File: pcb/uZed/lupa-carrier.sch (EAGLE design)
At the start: 94 parts, among them J5 HDMI-TYPE-A-RECEPTICALFCI1002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, J6 HDMI-TYPE-A-RECEPTICALFCI1002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, K1 694108105102

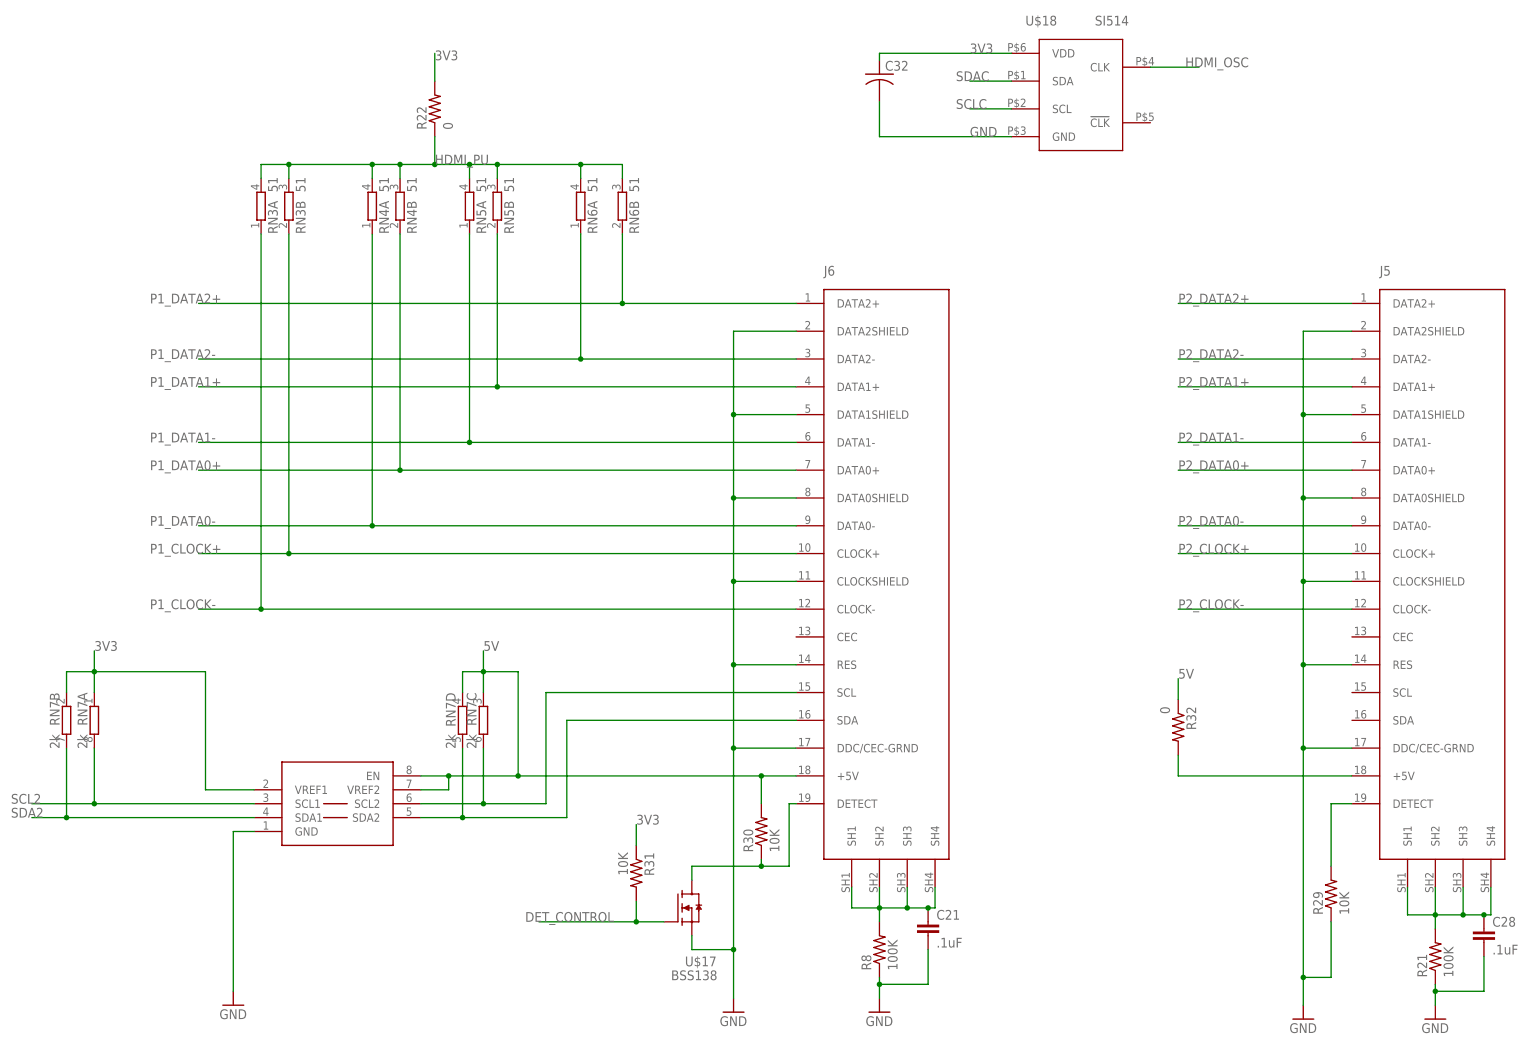
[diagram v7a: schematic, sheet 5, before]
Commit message: routing completed. needs double check before ordering from fab
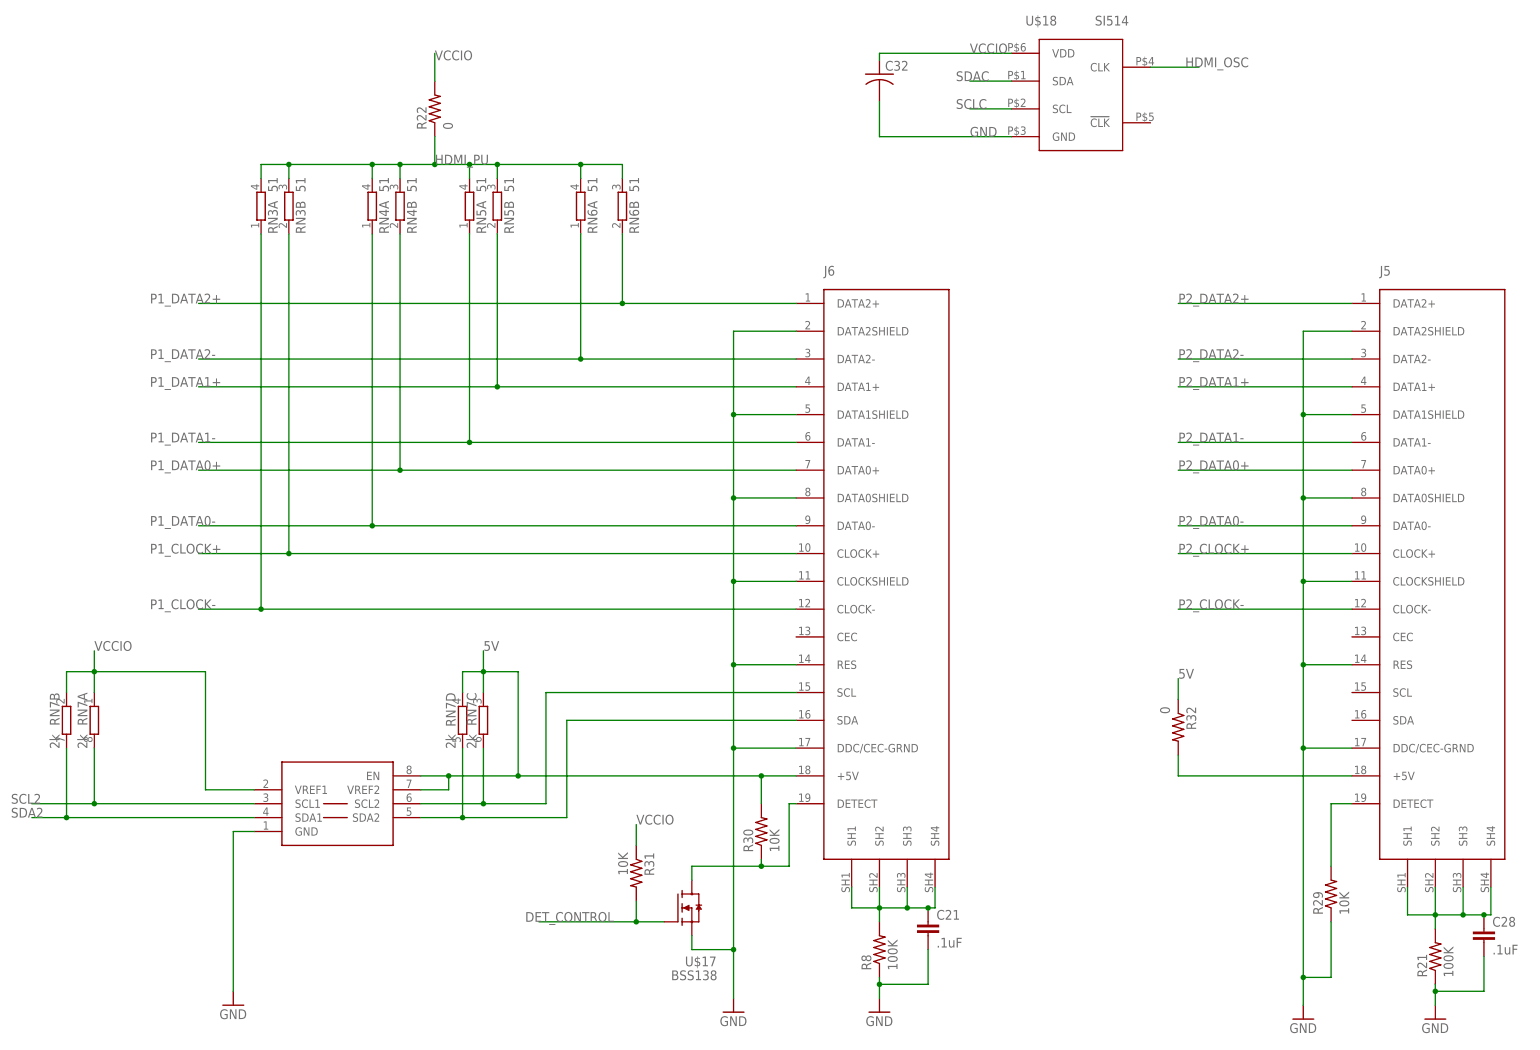
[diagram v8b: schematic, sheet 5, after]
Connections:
- removed net 3V3: C32.1, PCA9306.VREF1, R22.2, R31.1, RN7A.1, RN7B.1, U$18.VDD
- net SCLC: now also JX1.P$19
- net SDAC: now also JX1.P$17
- net VCCIO: now also C32.1, PCA9306.VREF1, R22.2, R31.1, RN7A.1, RN7B.1, U$18.VDD
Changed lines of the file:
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@@
+</segment>
+</net>
+<net name="SDAC" class="0">
+<segment>
+<pinref part="JX1" gate="G$1" pin="P$17"/>
+<wire x1="170.18" y1="129.54" x2="187.96" y2="129.54" width="0.1524" layer="91"/>
+<label x="187.96" y="129.54" size="1.778" layer="95"/>
+</segment>
+</net>
+<net name="SCLC" class="0">
+<segment>
+<pinref part="JX1" gate="G$1" pin="P$19"/>
+<wire x1="170.18" y1="127" x2="187.96" y2="127" width="0.1524" layer="91"/>
+<label x="187.96" y="127" size="1.778" layer="95"/>
 </segment>
 </net>
@@
 </segment>
 </net>
-<net name="3V3" class="0">
-<segment>
-<pinref part="R22" gate="G$1" pin="2"/>
-<wire x1="82.55" y1="185.42" x2="82.55" y2="190.5" width="0.1524" layer="91"/>
-<label x="82.55" y="189.23" size="1.778" layer="95"/>
-</segment>
-<segment>
-<pinref part="PCA9306" gate="G$1" pin="VREF1"/>
-<wire x1="49.53" y1="55.88" x2="40.64" y2="55.88" width="0.1524" layer="91"/>
-<wire x1="15.24" y1="73.66" x2="15.24" y2="77.47" width="0.1524" layer="91"/>
-<wire x1="15.24" y1="77.47" x2="20.32" y2="77.47" width="0.1524" layer="91"/>
-<wire x1="20.32" y1="77.47" x2="20.32" y2="73.66" width="0.1524" layer="91"/>
-<wire x1="20.32" y1="77.47" x2="40.64" y2="77.47" width="0.1524" layer="91"/>
-<wire x1="40.64" y1="77.47" x2="40.64" y2="55.88" width="0.1524" layer="91"/>
-<pinref part="RN7" gate="B" pin="1"/>
-<pinref part="RN7" gate="A" pin="1"/>
-<junction x="20.32" y="77.47"/>
-<wire x1="20.32" y1="77.47" x2="20.32" y2="81.28" width="0.1524" layer="91"/>
-<label x="20.32" y="81.28" size="1.778" layer="95"/>
-</segment>
-<segment>
-<pinref part="R31" gate="G$1" pin="1"/>
-<wire x1="119.38" y1="45.72" x2="119.38" y2="49.53" width="0.1524" layer="91"/>
-<label x="119.38" y="49.53" size="1.778" layer="95"/>
-</segment>
-<segment>
-<pinref part="U$18" gate="G$1" pin="VDD"/>
-<label x="180.34" y="190.5" size="1.778" layer="95"/>
-<wire x1="187.96" y1="190.5" x2="163.83" y2="190.5" width="0.1524" layer="91"/>
-<pinref part="C32" gate="G$1" pin="1"/>
-<wire x1="163.83" y1="190.5" x2="163.83" y2="189.23" width="0.1524" layer="91"/>
-</segment>
-</net>
 <net name="N$17" class="0">
 <segment>
@@
 </segment>
 </net>
+<net name="VCCIO" class="0">
+<segment>
+<pinref part="U$18" gate="G$1" pin="VDD"/>
+<label x="180.34" y="190.5" size="1.778" layer="95"/>
+<wire x1="187.96" y1="190.5" x2="163.83" y2="190.5" width="0.1524" layer="91"/>
+<pinref part="C32" gate="G$1" pin="1"/>
+<wire x1="163.83" y1="190.5" x2="163.83" y2="189.23" width="0.1524" layer="91"/>
+</segment>
+<segment>
+<pinref part="PCA9306" gate="G$1" pin="VREF1"/>
+<wire x1="49.53" y1="55.88" x2="40.64" y2="55.88" width="0.1524" layer="91"/>
+<wire x1="15.24" y1="73.66" x2="15.24" y2="77.47" width="0.1524" layer="91"/>
+<wire x1="15.24" y1="77.47" x2="20.32" y2="77.47" width="0.1524" layer="91"/>
+<wire x1="20.32" y1="77.47" x2="20.32" y2="73.66" width="0.1524" layer="91"/>
+<wire x1="20.32" y1="77.47" x2="40.64" y2="77.47" width="0.1524" layer="91"/>
+<wire x1="40.64" y1="77.47" x2="40.64" y2="55.88" width="0.1524" layer="91"/>
+<pinref part="RN7" gate="B" pin="1"/>
+<pinref part="RN7" gate="A" pin="1"/>
+<junction x="20.32" y="77.47"/>
+<wire x1="20.32" y1="77.47" x2="20.32" y2="81.28" width="0.1524" layer="91"/>
+<label x="20.32" y="81.28" size="1.778" layer="95"/>
+</segment>
+<segment>
+<pinref part="R31" gate="G$1" pin="1"/>
+<wire x1="119.38" y1="45.72" x2="119.38" y2="49.53" width="0.1524" layer="91"/>
+<label x="119.38" y="49.53" size="1.778" layer="95"/>
+</segment>
+<segment>
+<pinref part="R22" gate="G$1" pin="2"/>
+<wire x1="82.55" y1="185.42" x2="82.55" y2="190.5" width="0.1524" layer="91"/>
+<label x="82.55" y="189.23" size="1.778" layer="95"/>
+</segment>
+</net>
